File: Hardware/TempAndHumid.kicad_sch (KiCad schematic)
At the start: 1 part, among them U3 HDC2010YPAR

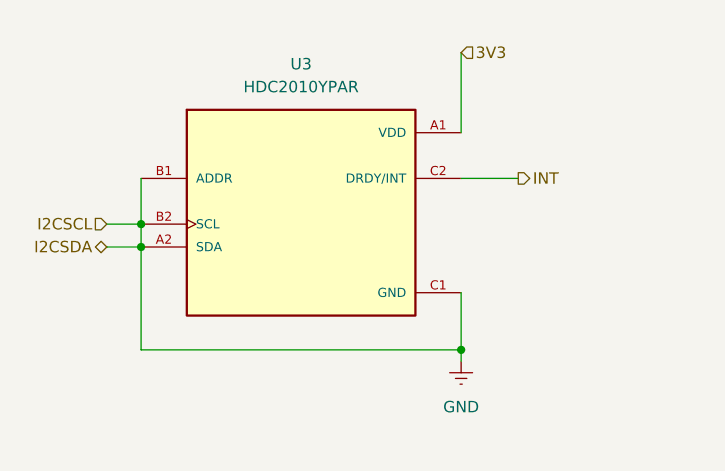
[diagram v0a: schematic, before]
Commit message: Add bypass cap to humid, and fix add grounding
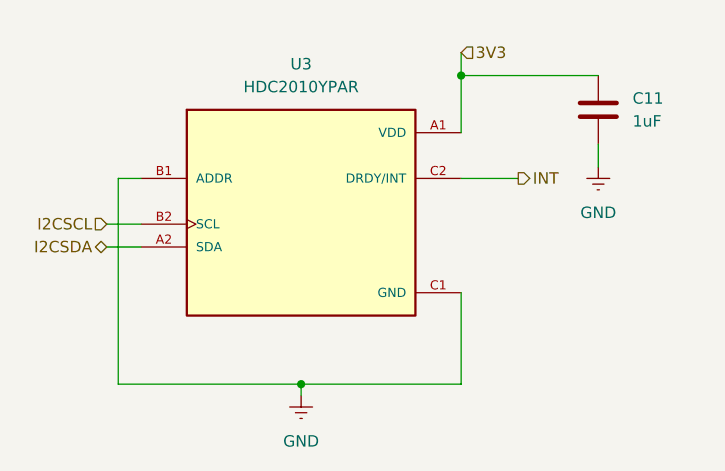
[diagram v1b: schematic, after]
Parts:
- added C11: 1uF, symbol Device:C
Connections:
- net 3V3: now also C11.1
- net GND: now also C11.2; no longer U3.A2 (SDA), U3.B2 (SCL)
- new net I2CSCL: U3.B2 (SCL)
- new net I2CSDA: U3.A2 (SDA)
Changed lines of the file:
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@@
 	(paper "A4")
 	(junction
-		(at 111.76 92.71)
+		(at 147.32 76.2)
 		(diameter 0)
 		(color 0 0 0 0)
 	)
 	(junction
-		(at 147.32 106.68)
+		(at 129.54 110.49)
 		(diameter 0)
 		(color 0 0 0 0)
 	)
-	(junction
-		(at 111.76 95.25)
-		(diameter 0)
-		(color 0 0 0 0)
+	(wire
+		(pts
+			(xy 111.76 87.63) (xy 109.22 87.63)
+		)
+		(stroke
+			(width 0)
+			(type default)
+		)
 	)
 	(wire
@@
 	(wire
 		(pts
-			(xy 147.32 73.66) (xy 147.32 82.55)
-		)
-		(stroke
-			(width 0)
-			(type default)
-		)
-	)
-	(wire
-		(pts
-			(xy 111.76 92.71) (xy 111.76 95.25)
+			(xy 147.32 73.66) (xy 147.32 76.2)
+		)
+		(stroke
+			(width 0)
+			(type default)
+		)
+	)
+	(wire
+		(pts
+			(xy 147.32 76.2) (xy 162.56 76.2)
 		)
 		(stroke
@@
 	(wire
 		(pts
-			(xy 147.32 100.33) (xy 147.32 106.68)
-		)
-		(stroke
-			(width 0)
-			(type default)
-		)
-	)
-	(wire
-		(pts
-			(xy 111.76 106.68) (xy 147.32 106.68)
-		)
-		(stroke
-			(width 0)
-			(type default)
-		)
-	)
-	(wire
-		(pts
-			(xy 111.76 95.25) (xy 111.76 106.68)
-		)
-		(stroke
-			(width 0)
-			(type default)
-		)
-	)
-	(wire
-		(pts
-			(xy 147.32 106.68) (xy 147.32 107.95)
-		)
-		(stroke
-			(width 0)
-			(type default)
-		)
-	)
-	(wire
-		(pts
-			(xy 111.76 87.63) (xy 111.76 92.71)
+			(xy 129.54 111.76) (xy 129.54 110.49)
+		)
+		(stroke
+			(width 0)
+			(type default)
+		)
+	)
+	(wire
+		(pts
+			(xy 129.54 110.49) (xy 147.32 110.49)
+		)
+		(stroke
+			(width 0)
+			(type default)
+		)
+	)
+	(wire
+		(pts
+			(xy 109.22 110.49) (xy 129.54 110.49)
+		)
+		(stroke
+			(width 0)
+			(type default)
+		)
+	)
+	(wire
+		(pts
+			(xy 147.32 100.33) (xy 147.32 110.49)
+		)
+		(stroke
+			(width 0)
+			(type default)
+		)
+	)
+	(wire
+		(pts
+			(xy 162.56 86.36) (xy 162.56 83.82)
+		)
+		(stroke
+			(width 0)
+			(type default)
+		)
+	)
+	(wire
+		(pts
+			(xy 147.32 76.2) (xy 147.32 82.55)
+		)
+		(stroke
+			(width 0)
+			(type default)
+		)
+	)
+	(wire
+		(pts
+			(xy 109.22 87.63) (xy 109.22 110.49)
 		)
 		(stroke
@@
 	(symbol
 		(lib_id "Peanut:GND")
-		(at 147.32 107.95 0)
+		(at 129.54 111.76 0)
 		(unit 1)
 		(exclude_from_sim no)
@@
 		(fields_autoplaced yes)
 		(property "Reference" "#PWR013"
-			(at 147.32 114.3 0)
+			(at 129.54 118.11 0)
 			(effects
 				(font
@@
 		)
 		(property "Value" "GND"
-			(at 147.32 113.03 0)
+			(at 129.54 116.84 0)
 			(effects
 				(font
@@
 		)
 		(property "Footprint" ""
-			(at 147.32 107.95 0)
+			(at 129.54 111.76 0)
 			(effects
 				(font
@@
 		)
 		(property "Datasheet" ""
-			(at 147.32 107.95 0)
+			(at 129.54 111.76 0)
 			(effects
 				(font
@@
 		)
 		(property "Description" "Power symbol creates a global label with name \"GNDREF\" , reference supply ground"
-			(at 147.32 107.95 0)
+			(at 129.54 111.76 0)
 			(effects
 				(font
@@
 					(unit 1)
 				)
+			)
+		)
+	)
+	(symbol
+		(lib_id "Peanut:GND")
+		(at 162.56 86.36 0)
+		(unit 1)
+		(exclude_from_sim no)
+		(in_bom yes)
+		(on_board yes)
+		(dnp no)
+		(fields_autoplaced yes)
+		(property "Reference" "#PWR014"
+			(at 162.56 92.71 0)
+			(effects
+				(font
+					(size 1.27 1.27)
+				)
+				(hide yes)
+			)
+		)
+		(property "Value" "GND"
+			(at 162.56 91.44 0)
+			(effects
+				(font
+					(size 1.27 1.27)
+				)
+			)
+		)
+		(property "Footprint" ""
+			(at 162.56 86.36 0)
+			(effects
+				(font
+					(size 1.27 1.27)
+				)
+				(hide yes)
+			)
+		)
+		(property "Datasheet" ""
+			(at 162.56 86.36 0)
+			(effects
+				(font
+					(size 1.27 1.27)
+				)
+				(hide yes)
+			)
+		)
+		(property "Description" "Power symbol creates a global label with name \"GNDREF\" , reference supply ground"
+			(at 162.56 86.36 0)
+			(effects
+				(font
+					(size 1.27 1.27)
+				)
+				(hide yes)
+			)
+		)
+		(pin "1"
+		)
+		(instances
+			(project "Peanut"
+				(path "/298ef215-2a76-4225-b9ba-26c57869f278/2a7593ef-e0f0-4226-9957-5319b4cb98cf"
+					(reference "#PWR014")
+					(unit 1)
+				)
+			)
+		)
+	)
+	(symbol
+		(lib_id "Device:C")
+		(at 162.56 80.01 0)
+		(unit 1)
+		(exclude_from_sim no)
+		(in_bom yes)
+		(on_board yes)
+		(dnp no)
+		(fields_autoplaced yes)
+		(property "Reference" "C11"
+			(at 166.37 78.7399 0)
+			(effects
+				(font
+					(size 1.27 1.27)
+				)
+				(justify left)
+			)
+		)
+		(property "Value" "1uF"
+			(at 166.37 81.2799 0)
+			(effects
+				(font
+					(size 1.27 1.27)
+				)
+				(justify left)
+			)
+		)
+		(property "Footprint" ""
+			(at 163.5252 83.82 0)
+			(effects
+				(font
+					(size 1.27 1.27)
+				)
+				(hide yes)
+			)
+		)
+		(property "Datasheet" "~"
+			(at 162.56 80.01 0)
+			(effects
+				(font
+					(size 1.27 1.27)
+				)
+				(hide yes)
+			)
+		)
+		(property "Description" "Unpolarized capacitor"
+			(at 162.56 80.01 0)
+			(effects
+				(font
+					(size 1.27 1.27)
+				)
+				(hide yes)
+			)
+		)
+		(pin "1"
+		)
+		(pin "2"
+		)
+		(instances
+			(project "Peanut"
+				(path "/298ef215-2a76-4225-b9ba-26c57869f278/2a7593ef-e0f0-4226-9957-5319b4cb98cf"
+					(reference "C11")
+					(unit 1)
+				)

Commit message: Use tags for nets, apply netgroups, mess around in pcb view
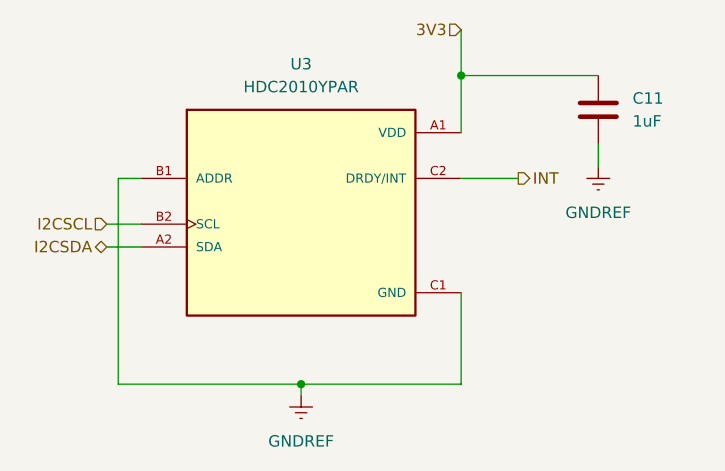
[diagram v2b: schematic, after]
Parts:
- C11: footprint (none) -> Capacitor_SMD:C_0201_0603Metric
- U3: footprint Snapeda:HDC2010YPAR_BGA6C100X50P2X3_HDC2010YPAR -> Snapeda:BGA6C100X50P2X3_HDC2010YPAR
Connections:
- net GND renamed GNDREF
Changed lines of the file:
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@@
 	(wire
 		(pts
-			(xy 147.32 73.66) (xy 147.32 76.2)
+			(xy 147.32 71.12) (xy 147.32 76.2)
 		)
 		(stroke
@@
 	(hierarchical_label "3V3"
 		(shape input)
-		(at 147.32 73.66 0)
+		(at 147.32 71.12 180)
 		(fields_autoplaced yes)
 		(effects
@@
 				(size 1.27 1.27)
 			)
-			(justify left)
+			(justify right)
 		)
 	)
@@
 	)
 	(symbol
-		(lib_id "Peanut:GND")
-		(at 129.54 111.76 0)
-		(unit 1)
-		(exclude_from_sim no)
-		(in_bom yes)
-		(on_board yes)
-		(dnp no)
-		(fields_autoplaced yes)
-		(property "Reference" "#PWR013"
-			(at 129.54 118.11 0)
-			(effects
-				(font
-					(size 1.27 1.27)
-				)
-				(hide yes)
-			)
-		)
-		(property "Value" "GND"
-			(at 129.54 116.84 0)
-			(effects
-				(font
-					(size 1.27 1.27)
-				)
-			)
-		)
-		(property "Footprint" ""
-			(at 129.54 111.76 0)
-			(effects
-				(font
-					(size 1.27 1.27)
-				)
-				(hide yes)
-			)
-		)
-		(property "Datasheet" ""
-			(at 129.54 111.76 0)
-			(effects
-				(font
-					(size 1.27 1.27)
-				)
-				(hide yes)
-			)
-		)
-		(property "Description" "Power symbol creates a global label with name \"GNDREF\" , reference supply ground"
-			(at 129.54 111.76 0)
-			(effects
-				(font
-					(size 1.27 1.27)
-				)
-				(hide yes)
-			)
-		)
-		(pin "1"
-		)
-		(instances
-			(project "Peanut"
-				(path "/298ef215-2a76-4225-b9ba-26c57869f278/2a7593ef-e0f0-4226-9957-5319b4cb98cf"
-					(reference "#PWR013")
-					(unit 1)
-				)
-			)
-		)
-	)
-	(symbol
-		(lib_id "Peanut:GND")
+		(lib_id "PartsLib:GNDREF")
 		(at 162.56 86.36 0)
 		(unit 1)
@@
 			)
 		)
-		(property "Value" "GND"
+		(property "Value" "GNDREF"
 			(at 162.56 91.44 0)
 			(effects
@@
 			)
 		)
-		(property "Footprint" ""
+		(property "Footprint" "Capacitor_SMD:C_0201_0603Metric"
 			(at 163.5252 83.82 0)
 			(effects
@@
 			)
 		)
-		(property "Footprint" "Snapeda:HDC2010YPAR_BGA6C100X50P2X3_HDC2010YPAR"
+		(property "Footprint" "Snapeda:BGA6C100X50P2X3_HDC2010YPAR"
 			(at 129.286 77.216 0)
 			(effects
@@
 					(unit 1)
 				)
+			)
+		)
+	)
+	(symbol
+		(lib_id "PartsLib:GNDREF")
+		(at 129.54 111.76 0)
+		(unit 1)
+		(exclude_from_sim no)
+		(in_bom yes)
+		(on_board yes)
+		(dnp no)
+		(fields_autoplaced yes)
+		(property "Reference" "#PWR013"
+			(at 129.54 118.11 0)
+			(effects
+				(font
+					(size 1.27 1.27)
+				)
+				(hide yes)
+			)
+		)
+		(property "Value" "GNDREF"
+			(at 129.54 116.84 0)
+			(effects
+				(font
+					(size 1.27 1.27)
+				)
+			)
+		)
+		(property "Footprint" ""
+			(at 129.54 111.76 0)
+			(effects
+				(font
+					(size 1.27 1.27)
+				)
+				(hide yes)
+			)
+		)
+		(property "Datasheet" ""
+			(at 129.54 111.76 0)
+			(effects
+				(font
+					(size 1.27 1.27)
+				)
+				(hide yes)
+			)
+		)
+		(property "Description" "Power symbol creates a global label with name \"GNDREF\" , reference supply ground"
+			(at 129.54 111.76 0)
+			(effects
+				(font
+					(size 1.27 1.27)
+				)
+				(hide yes)
+			)
+		)
+		(pin "1"
+		)
+		(instances
+			(project "Peanut"
+				(path "/298ef215-2a76-4225-b9ba-26c57869f278/2a7593ef-e0f0-4226-9957-5319b4cb98cf"
+					(reference "#PWR013")
+					(unit 1)
+				)

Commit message: Use Peanut symbols, fix ERC errors, progress on DAC & Pressure
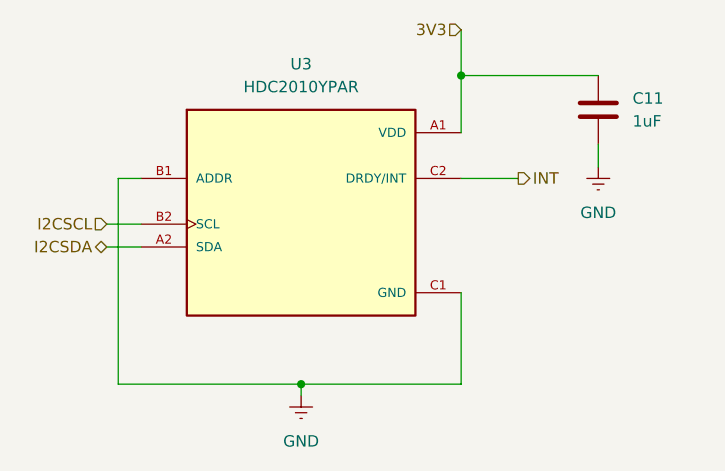
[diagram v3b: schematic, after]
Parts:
- U3: footprint Snapeda:BGA6C100X50P2X3_HDC2010YPAR -> Peanut:HDC2010YPAR
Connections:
- net GNDREF renamed GND
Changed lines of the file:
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@@
 	)
 	(symbol
-		(lib_id "PartsLib:GNDREF")
+		(lib_id "Peanut:GND")
+		(at 129.54 111.76 0)
+		(unit 1)
+		(exclude_from_sim no)
+		(in_bom yes)
+		(on_board yes)
+		(dnp no)
+		(fields_autoplaced yes)
+		(property "Reference" "#PWR013"
+			(at 129.54 118.11 0)
+			(effects
+				(font
+					(size 1.27 1.27)
+				)
+				(hide yes)
+			)
+		)
+		(property "Value" "GND"
+			(at 129.54 116.84 0)
+			(effects
+				(font
+					(size 1.27 1.27)
+				)
+			)
+		)
+		(property "Footprint" ""
+			(at 129.54 111.76 0)
+			(effects
+				(font
+					(size 1.27 1.27)
+				)
+				(hide yes)
+			)
+		)
+		(property "Datasheet" ""
+			(at 129.54 111.76 0)
+			(effects
+				(font
+					(size 1.27 1.27)
+				)
+				(hide yes)
+			)
+		)
+		(property "Description" ""
+			(at 129.54 120.396 0)
+			(effects
+				(font
+					(size 1.27 1.27)
+				)
+				(hide yes)
+			)
+		)
+		(pin "1"
+		)
+		(instances
+			(project "Peanut"
+				(path "/298ef215-2a76-4225-b9ba-26c57869f278/2a7593ef-e0f0-4226-9957-5319b4cb98cf"
+					(reference "#PWR013")
+					(unit 1)
+				)
+			)
+		)
+	)
+	(symbol
+		(lib_id "Peanut:GND")
 		(at 162.56 86.36 0)
 		(unit 1)
@@
 			)
 		)
-		(property "Value" "GNDREF"
+		(property "Value" "GND"
 			(at 162.56 91.44 0)
 			(effects
@@
 			)
 		)
-		(property "Description" "Power symbol creates a global label with name \"GNDREF\" , reference supply ground"
-			(at 162.56 86.36 0)
+		(property "Description" ""
+			(at 162.56 94.996 0)
 			(effects
 				(font
@@
 			)
 		)
-		(property "Footprint" "Snapeda:BGA6C100X50P2X3_HDC2010YPAR"
+		(property "Footprint" "Peanut:HDC2010YPAR"
 			(at 129.286 77.216 0)
 			(effects
@@
 					(unit 1)
 				)
-			)
-		)
-	)
-	(symbol
-		(lib_id "PartsLib:GNDREF")
-		(at 129.54 111.76 0)
-		(unit 1)
-		(exclude_from_sim no)
-		(in_bom yes)
-		(on_board yes)
-		(dnp no)
-		(fields_autoplaced yes)
-		(property "Reference" "#PWR013"
-			(at 129.54 118.11 0)
-			(effects
-				(font
-					(size 1.27 1.27)
-				)
-				(hide yes)
-			)
-		)
-		(property "Value" "GNDREF"
-			(at 129.54 116.84 0)
-			(effects
-				(font
-					(size 1.27 1.27)
-				)
-			)
-		)
-		(property "Footprint" ""
-			(at 129.54 111.76 0)
-			(effects
-				(font
-					(size 1.27 1.27)
-				)
-				(hide yes)
-			)
-		)
-		(property "Datasheet" ""
-			(at 129.54 111.76 0)
-			(effects
-				(font
-					(size 1.27 1.27)
-				)
-				(hide yes)
-			)
-		)
-		(property "Description" "Power symbol creates a global label with name \"GNDREF\" , reference supply ground"
-			(at 129.54 111.76 0)
-			(effects
-				(font
-					(size 1.27 1.27)
-				)
-				(hide yes)
-			)
-		)
-		(pin "1"
-		)
-		(instances
-			(project "Peanut"
-				(path "/298ef215-2a76-4225-b9ba-26c57869f278/2a7593ef-e0f0-4226-9957-5319b4cb98cf"
-					(reference "#PWR013")
-					(unit 1)
-				)

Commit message: Fully wired board!
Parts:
- C11: footprint Capacitor_SMD:C_0201_0603Metric -> Resistor_SMD:R_01005_0402Metric; symbol Device:C -> Peanut:C
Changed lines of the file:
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@@
 	)
 	(symbol
-		(lib_id "Device:C")
+		(lib_id "Peanut:C")
 		(at 162.56 80.01 0)
 		(unit 1)
@@
 			)
 		)
-		(property "Footprint" "Capacitor_SMD:C_0201_0603Metric"
+		(property "Footprint" "Resistor_SMD:R_01005_0402Metric"
 			(at 163.5252 83.82 0)
 			(effects

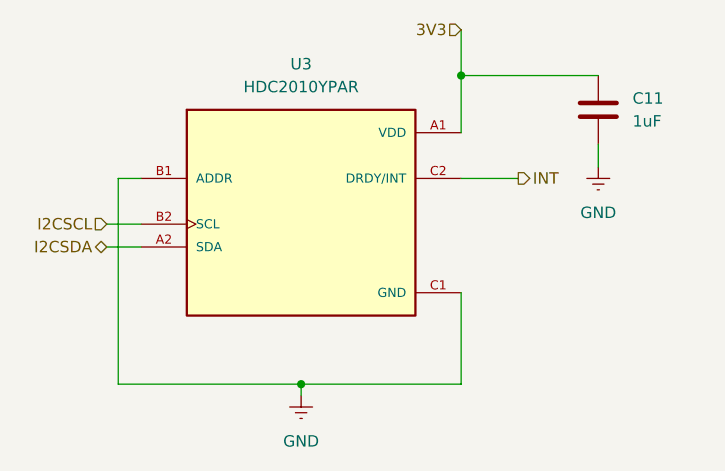
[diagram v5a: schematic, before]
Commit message: Initial OS architecture, and updated PCB work After a joint planning session, designed and architected OS structure: ``` src/ |- os: Audio, Accelerometer, Humidity, etc |- drivers: I2C interfaces, per-chip ```
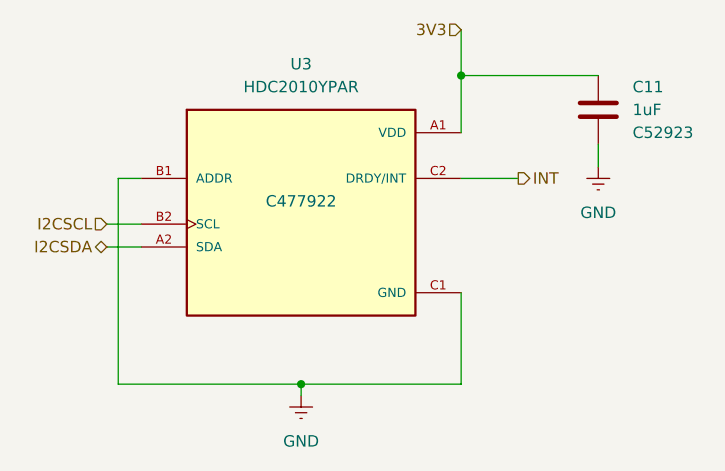
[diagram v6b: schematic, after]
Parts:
- C11: footprint Resistor_SMD:R_01005_0402Metric -> Capacitor_SMD:C_0402_1005Metric; symbol Peanut:C -> Peanut:C 1uF; LCSC (none) -> C52923
- U3: LCSC (none) -> C477922
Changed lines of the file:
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@@
 	)
 	(symbol
-		(lib_id "Peanut:C")
+		(lib_id "Peanut:C 1uF")
 		(at 162.56 80.01 0)
 		(unit 1)
@@
 		(fields_autoplaced yes)
 		(property "Reference" "C11"
-			(at 166.37 78.7399 0)
+			(at 166.37 77.4699 0)
 			(effects
 				(font
@@
 		)
 		(property "Value" "1uF"
-			(at 166.37 81.2799 0)
+			(at 166.37 80.0099 0)
 			(effects
 				(font
@@
 			)
 		)
-		(property "Footprint" "Resistor_SMD:R_01005_0402Metric"
+		(property "Footprint" "Capacitor_SMD:C_0402_1005Metric"
 			(at 163.5252 83.82 0)
 			(effects
@@
 				)
 				(hide yes)
+			)
+		)
+		(property "LCSC" "C52923"
+			(at 166.37 82.5499 0)
+			(effects
+				(font
+					(size 1.27 1.27)
+				)
+				(justify left)
 			)
 		)
@@
 			)
 		)
+		(property "LCSC" "C477922"
+			(at 129.54 90.17 0)
+			(effects
+				(font
+					(size 1.27 1.27)
+				)
+			)
+		)
